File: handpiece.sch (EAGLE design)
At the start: 27 parts, among them IC1 MEGA8-P

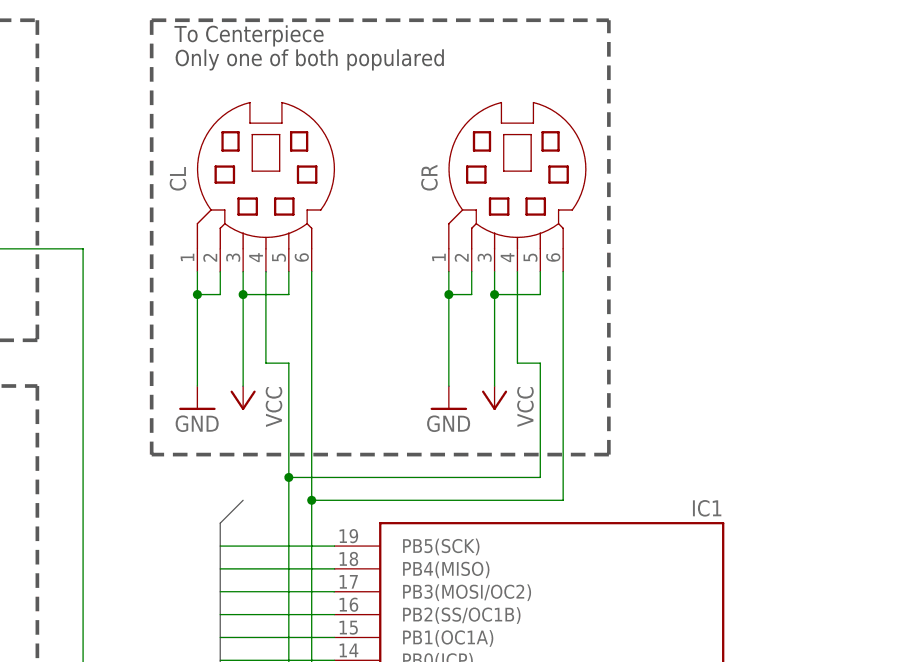
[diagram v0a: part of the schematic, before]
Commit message: exchange minidin connectors with raw soldering pads and strain-releive holes
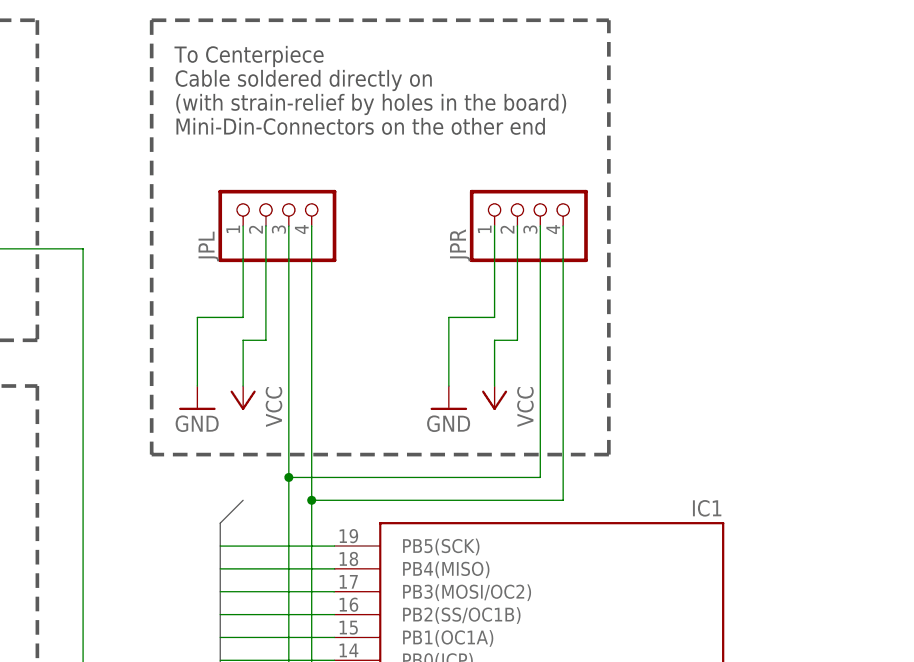
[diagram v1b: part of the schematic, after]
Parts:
- removed CL, CR: (no value), con-yamaichi:MD06SS
- added JPL, JPR: (no value), pinhead:PINHD-1X4
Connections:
- net GND: now also JPL.1, JPR.1; no longer CL.1, CL.2, CR.1, CR.2
- net SCL: now also JPL.4, JPR.4; no longer CL.6, CR.6
- net SDA: now also JPL.3, JPR.3; no longer CL.4, CR.4
- net VCC: now also JPL.2, JPR.2; no longer CL.3, CL.5, CR.3, CR.5
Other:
- note added: "To Centerpiece Cable soldered directly on (with strain-relief by holes in the board) Mini-Din-Connectors on the other end"
- note removed: "To Centerpiece Only one of both populared"
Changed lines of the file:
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@@
 <?xml version="1.0" encoding="utf-8"?>
 <!DOCTYPE eagle SYSTEM "eagle.dtd">
-<eagle version="6.5.0">
+<eagle version="6.4">
 <drawing>
 <settings>
@@
 <setting verticaltext="up"/>
 </settings>
-<grid distance="0.1" unitdist="inch" unit="inch" style="lines" multiple="1" display="yes" altdistance="0.01" altunitdist="inch" altunit="inch"/>
+<grid distance="0.1" unitdist="inch" unit="inch" style="lines" multiple="1" display="no" altdistance="0.01" altunitdist="inch" altunit="inch"/>
 <layers>
 <layer number="1" name="Top" color="4" fill="1" visible="no" active="no"/>
@@
 <part name="GND16" library="supply1" deviceset="GND" device=""/>
 <part name="GND17" library="supply1" deviceset="GND" device=""/>
-<part name="CL" library="con-yamaichi" deviceset="MD06SS" device=""/>
 <part name="GND18" library="supply1" deviceset="GND" device=""/>
 <part name="P+6" library="supply1" deviceset="VCC" device=""/>
@@
 <part name="GND19" library="supply1" deviceset="GND" device=""/>
 <part name="GND20" library="supply1" deviceset="GND" device=""/>
-<part name="CR" library="con-yamaichi" deviceset="MD06SS" device=""/>
 <part name="GND21" library="supply1" deviceset="GND" device=""/>
 <part name="P+5" library="supply1" deviceset="VCC" device=""/>
+<part name="JPL" library="pinhead" deviceset="PINHD-1X4" device=""/>
+<part name="JPR" library="pinhead" deviceset="PINHD-1X4" device=""/>
 </parts>
 <sheets>
@@
 <text x="96.52" y="-2.54" size="1.778" layer="97">Only populated on Left-Handpiece</text>
 <text x="5.08" y="-2.54" size="1.778" layer="97">Only populated on Right-Handpiece</text>
-<text x="152.4" y="99.06" size="1.778" layer="97">To Centerpiece
-Only one of both populared</text>
+<text x="152.4" y="91.44" size="1.778" layer="97">To Centerpiece
+Cable soldered directly on
+(with strain-relief by holes in the board)
+Mini-Din-Connectors on the other end</text>
 <wire x1="149.86" y1="104.14" x2="200.66" y2="104.14" width="0.4064" layer="97" style="shortdash"/>
 <wire x1="200.66" y1="55.88" x2="200.66" y2="104.14" width="0.4064" layer="97" style="shortdash"/>
@@
 <instance part="GND16" gate="1" x="91.44" y="38.1" rot="R180"/>
 <instance part="GND17" gate="1" x="114.3" y="38.1" rot="R180"/>
-<instance part="CL" gate="G$1" x="162.56" y="86.36" rot="R90"/>
 <instance part="GND18" gate="1" x="154.94" y="60.96"/>
 <instance part="P+6" gate="VCC" x="160.02" y="60.96" rot="R180"/>
@@
 <instance part="GND19" gate="1" x="106.68" y="-20.32" rot="R90"/>
 <instance part="GND20" gate="1" x="129.54" y="-20.32" rot="R90"/>
-<instance part="CR" gate="G$1" x="190.5" y="86.36" rot="R90"/>
 <instance part="GND21" gate="1" x="182.88" y="60.96"/>
 <instance part="P+5" gate="VCC" x="187.96" y="60.96" rot="R180"/>
+<instance part="JPL" gate="A" x="165.1" y="83.82" rot="R90"/>
+<instance part="JPR" gate="A" x="193.04" y="83.82" rot="R90"/>
 </instances>
 <busses>
@@
 <segment>
 <pinref part="GND18" gate="1" pin="GND"/>
-<pinref part="CL" gate="G$1" pin="1"/>
-<wire x1="154.94" y1="63.5" x2="154.94" y2="73.66" width="0.1524" layer="91"/>
-<pinref part="CL" gate="G$1" pin="2"/>
-<wire x1="154.94" y1="73.66" x2="154.94" y2="76.2" width="0.1524" layer="91"/>
-<wire x1="157.48" y1="76.2" x2="157.48" y2="73.66" width="0.1524" layer="91"/>
-<wire x1="157.48" y1="73.66" x2="154.94" y2="73.66" width="0.1524" layer="91"/>
-<junction x="154.94" y="73.66"/>
+<wire x1="154.94" y1="63.5" x2="154.94" y2="71.12" width="0.1524" layer="91"/>
+<wire x1="154.94" y1="71.12" x2="160.02" y2="71.12" width="0.1524" layer="91"/>
+<wire x1="160.02" y1="71.12" x2="160.02" y2="81.28" width="0.1524" layer="91"/>
+<pinref part="JPL" gate="A" pin="1"/>
 </segment>
 <segment>
@@
 <segment>
 <pinref part="GND21" gate="1" pin="GND"/>
-<pinref part="CR" gate="G$1" pin="1"/>
-<wire x1="182.88" y1="63.5" x2="182.88" y2="73.66" width="0.1524" layer="91"/>
-<pinref part="CR" gate="G$1" pin="2"/>
-<wire x1="182.88" y1="73.66" x2="182.88" y2="76.2" width="0.1524" layer="91"/>
-<wire x1="182.88" y1="73.66" x2="185.42" y2="73.66" width="0.1524" layer="91"/>
-<wire x1="185.42" y1="73.66" x2="185.42" y2="76.2" width="0.1524" layer="91"/>
-<junction x="182.88" y="73.66"/>
+<wire x1="182.88" y1="63.5" x2="182.88" y2="71.12" width="0.1524" layer="91"/>
+<wire x1="182.88" y1="71.12" x2="187.96" y2="71.12" width="0.1524" layer="91"/>
+<wire x1="187.96" y1="71.12" x2="187.96" y2="81.28" width="0.1524" layer="91"/>
+<pinref part="JPR" gate="A" pin="1"/>
 </segment>
 </net>
@@
 </segment>
 <segment>
-<pinref part="CL" gate="G$1" pin="3"/>
 <pinref part="P+6" gate="VCC" pin="VCC"/>
-<wire x1="160.02" y1="76.2" x2="160.02" y2="73.66" width="0.1524" layer="91"/>
-<pinref part="CL" gate="G$1" pin="5"/>
-<wire x1="160.02" y1="73.66" x2="160.02" y2="63.5" width="0.1524" layer="91"/>
-<wire x1="165.1" y1="76.2" x2="165.1" y2="73.66" width="0.1524" layer="91"/>
-<wire x1="165.1" y1="73.66" x2="160.02" y2="73.66" width="0.1524" layer="91"/>
-<junction x="160.02" y="73.66"/>
+<wire x1="162.56" y1="81.28" x2="162.56" y2="68.58" width="0.1524" layer="91"/>
+<wire x1="162.56" y1="68.58" x2="160.02" y2="68.58" width="0.1524" layer="91"/>
+<wire x1="160.02" y1="68.58" x2="160.02" y2="63.5" width="0.1524" layer="91"/>
+<pinref part="JPL" gate="A" pin="2"/>
 </segment>
 <segment>
 <pinref part="P+5" gate="VCC" pin="VCC"/>
-<pinref part="CR" gate="G$1" pin="3"/>
-<wire x1="187.96" y1="63.5" x2="187.96" y2="73.66" width="0.1524" layer="91"/>
-<pinref part="CR" gate="G$1" pin="5"/>
-<wire x1="187.96" y1="73.66" x2="187.96" y2="76.2" width="0.1524" layer="91"/>
-<wire x1="187.96" y1="73.66" x2="193.04" y2="73.66" width="0.1524" layer="91"/>
-<wire x1="193.04" y1="73.66" x2="193.04" y2="76.2" width="0.1524" layer="91"/>
-<junction x="187.96" y="73.66"/>
+<wire x1="187.96" y1="63.5" x2="187.96" y2="68.58" width="0.1524" layer="91"/>
+<wire x1="187.96" y1="68.58" x2="190.5" y2="68.58" width="0.1524" layer="91"/>
+<wire x1="190.5" y1="68.58" x2="190.5" y2="81.28" width="0.1524" layer="91"/>
+<pinref part="JPR" gate="A" pin="2"/>
 </segment>
 </net>
@@
 <wire x1="170.18" y1="0" x2="167.64" y2="0" width="0.1524" layer="91"/>
 <wire x1="167.64" y1="0" x2="167.64" y2="50.8" width="0.1524" layer="91"/>
-<pinref part="CL" gate="G$1" pin="6"/>
-<pinref part="CR" gate="G$1" pin="6"/>
-<wire x1="167.64" y1="50.8" x2="167.64" y2="76.2" width="0.1524" layer="91"/>
-<wire x1="195.58" y1="76.2" x2="195.58" y2="50.8" width="0.1524" layer="91"/>
+<wire x1="167.64" y1="50.8" x2="167.64" y2="81.28" width="0.1524" layer="91"/>
+<wire x1="195.58" y1="81.28" x2="195.58" y2="50.8" width="0.1524" layer="91"/>
 <wire x1="195.58" y1="50.8" x2="167.64" y2="50.8" width="0.1524" layer="91"/>
 <junction x="167.64" y="50.8"/>
+<pinref part="JPL" gate="A" pin="4"/>
+<pinref part="JPR" gate="A" pin="4"/>
 </segment>
 </net>
@@
 <wire x1="170.18" y1="-2.54" x2="165.1" y2="-2.54" width="0.1524" layer="91"/>
 <wire x1="165.1" y1="-2.54" x2="165.1" y2="53.34" width="0.1524" layer="91"/>
-<pinref part="CL" gate="G$1" pin="4"/>
-<wire x1="165.1" y1="53.34" x2="165.1" y2="66.04" width="0.1524" layer="91"/>
-<wire x1="162.56" y1="76.2" x2="162.56" y2="66.04" width="0.1524" layer="91"/>
-<wire x1="165.1" y1="66.04" x2="162.56" y2="66.04" width="0.1524" layer="91"/>
-<pinref part="CR" gate="G$1" pin="4"/>
-<wire x1="190.5" y1="76.2" x2="190.5" y2="66.04" width="0.1524" layer="91"/>
-<wire x1="190.5" y1="66.04" x2="193.04" y2="66.04" width="0.1524" layer="91"/>
-<wire x1="193.04" y1="66.04" x2="193.04" y2="53.34" width="0.1524" layer="91"/>
+<wire x1="165.1" y1="53.34" x2="165.1" y2="81.28" width="0.1524" layer="91"/>
+<wire x1="193.04" y1="81.28" x2="193.04" y2="53.34" width="0.1524" layer="91"/>
 <wire x1="193.04" y1="53.34" x2="165.1" y2="53.34" width="0.1524" layer="91"/>
 <junction x="165.1" y="53.34"/>
-</segment>
-</net>
+<pinref part="JPL" gate="A" pin="3"/>
+<pinref part="JPR" gate="A" pin="3"/>
+</segment>
+</net>
